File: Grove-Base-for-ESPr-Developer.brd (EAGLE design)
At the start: 26 x 26 mm, 8 parts, among them J1 4P-2.0, J2 4P-2.0, J3 4P-2.0, J4 4P-2.0

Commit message: Replace the IO14 pin of the IO14 connector with IO15
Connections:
- net IO12: no longer J1.2
- net IO15: now also J1.2
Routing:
- net IO15: track 0.00 -> 19.8 mm
- net IO12: track 20.9 -> 11.7 mm
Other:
- board text added: "CC: BY-SA S. Kobayashi June 14, 2016"
- board text added: "D14 D15 3V3 GND"
- board text removed: "CC: BY-SA S. Kobayashi June 10, 2016"
- board text removed: "D14 D12 3V3 GND"
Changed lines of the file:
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@@
 <setting verticaltext="up"/>
 </settings>
-<grid distance="0.05" unitdist="inch" unit="inch" style="lines" multiple="1" display="yes" altdistance="0.0125" altunitdist="inch" altunit="inch"/>
+<grid distance="0.05" unitdist="inch" unit="inch" style="lines" multiple="1" display="yes" altdistance="0.005" altunitdist="inch" altunit="inch"/>
 <layers>
 <layer number="1" name="Top" color="4" fill="1" visible="yes" active="yes"/>
@@
 <text x="12.7" y="10.16" size="0.8128" layer="26" ratio="15" rot="MR0">CC: BY-SA
 S. Kobayashi
-June 10, 2016</text>
+June 14, 2016</text>
 <text x="3.81" y="18.0975" size="0.8128" layer="25" font="vector" ratio="15">D14
-D12
+D15
 3V3
 GND</text>
@@
 <signal name="IO15">
 <contactref element="JP1" pad="5"/>
+<contactref element="J1" pad="2"/>
+<wire x1="15.113" y1="21.336" x2="8.9916" y2="21.336" width="0.254" layer="1"/>
+<wire x1="16.1544" y1="22.3774" x2="15.113" y2="21.336" width="0.254" layer="1"/>
+<wire x1="16.7894" y1="22.3774" x2="16.1544" y2="22.3774" width="0.254" layer="1"/>
+<wire x1="23.0124" y1="16.1544" x2="16.7894" y2="22.3774" width="0.254" layer="1"/>
+<wire x1="23.0124" y1="15.0876" x2="23.0124" y2="16.1544" width="0.254" layer="1"/>
+<wire x1="24.13" y1="13.97" x2="23.0124" y2="15.0876" width="0.254" layer="1"/>
+<wire x1="8.9916" y1="21.336" x2="8.89" y2="21.32" width="0.1524" layer="1"/>
 </signal>
 <signal name="IO13">
@@
 <signal name="IO12">
 <contactref element="JP1" pad="7"/>
-<contactref element="J1" pad="2"/>
 <contactref element="J2" pad="1"/>
-<wire x1="12.8016" y1="17.3736" x2="16.4592" y2="17.3736" width="0.254" layer="1"/>
-<wire x1="8.9154" y1="21.2598" x2="12.8016" y2="17.3736" width="0.254" layer="1"/>
 <wire x1="16.4592" y1="17.3736" x2="16.51" y2="17.32" width="0.254" layer="1"/>
-<wire x1="8.9154" y1="21.2598" x2="8.89" y2="21.32" width="0.254" layer="1"/>
 <wire x1="24.003" y1="9.8298" x2="24.003" y2="8.9154" width="0.254" layer="1"/>
 <wire x1="16.6878" y1="17.145" x2="24.003" y2="9.8298" width="0.254" layer="1"/>

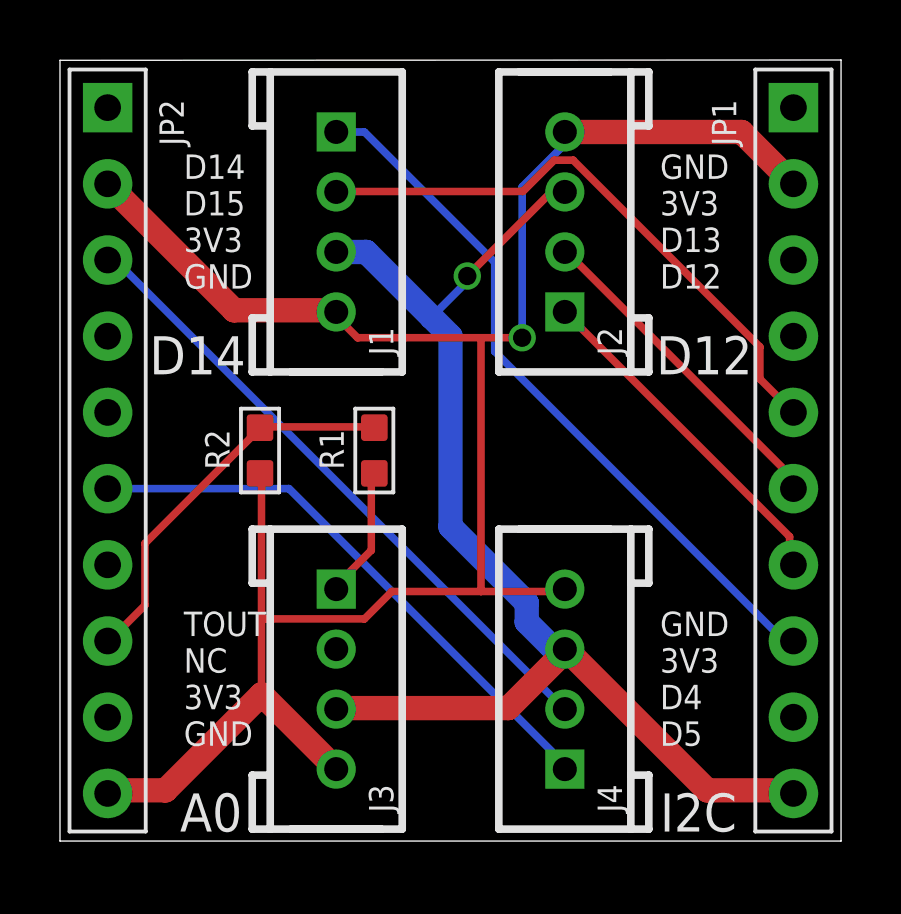
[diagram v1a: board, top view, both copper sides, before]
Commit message: Rotate 180 degree and revise labels
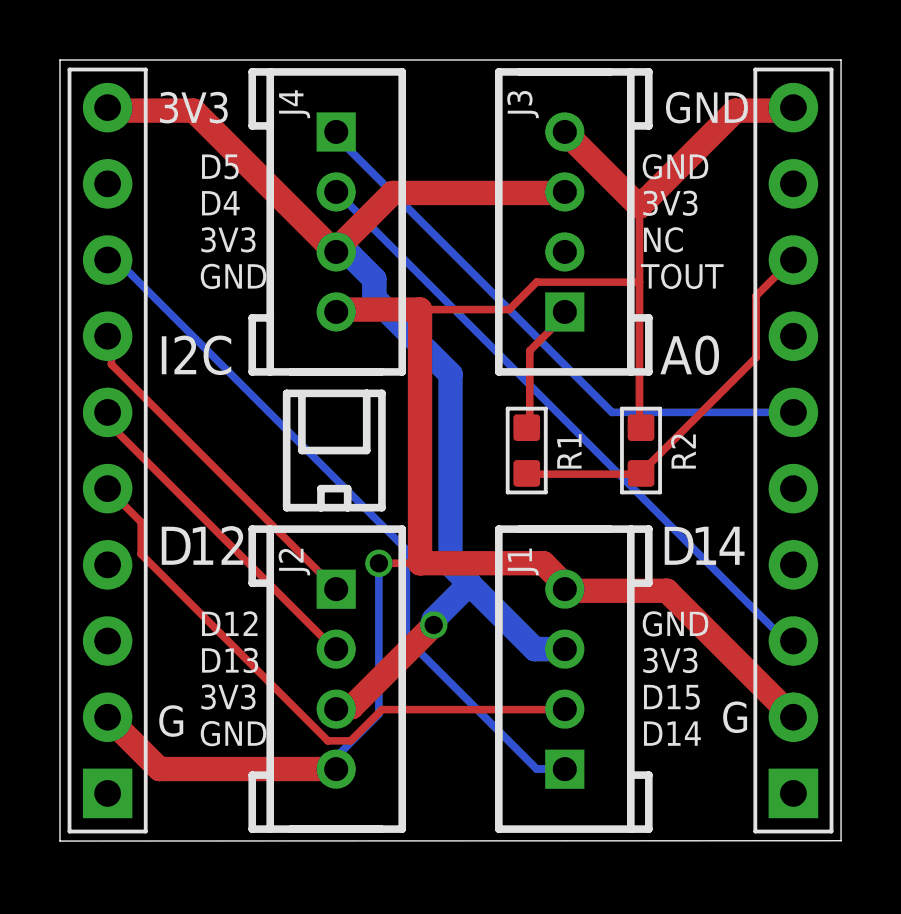
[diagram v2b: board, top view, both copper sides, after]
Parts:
- moved JP1 22.9 mm to (1.27, 12.7), turned to 180 degrees
- moved JP2 22.9 mm to (24.1, 12.7), turned to 180 degrees
- moved J1 17.0 mm to (16.5, 5.08), turned to 90 degrees
- moved J2 17.0 mm to (8.89, 5.08), turned to 270 degrees
- moved J3 17.0 mm to (16.5, 20.3), turned to 90 degrees
- moved J4 17.0 mm to (8.89, 20.3), turned to 270 degrees
- moved R2 12.7 mm to (19.1, 12.7), turned to 0 degrees
- moved R1 5.08 mm to (15.2, 12.7), turned to 180 degrees
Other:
- board text added: "1"
- board text added: "2"
- board text added: "3V3"
- board text added: "4"
- board text added: "CC: BY-SA S. Kobayashi June 20 2016"
- board text added: "D"
- board text added: "D12 D13 3V3 GND"
- board text added: "D5 D4 3V3 GND"
- board text added: "G"
- board text added: "GND"
- board text added: "GND 3V3 D15 D14"
- board text added: "GND 3V3 NC TOUT"
- board text removed: "CC: BY-SA S. Kobayashi June 14, 2016"
- board text removed: "D12"
- board text removed: "D14"
- board text removed: "D14 D15 3V3 GND"
- board text removed: "GND 3V3 D13 D12"
- board text removed: "GND 3V3 D4 D5"
- board text removed: "TOUT NC 3V3 GND"
